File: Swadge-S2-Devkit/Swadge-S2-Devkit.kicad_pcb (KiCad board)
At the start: 2 copper layers, 99.9 x 99.9 mm, 80 parts, among them J1 USB_B_Micro, J2 Conn_01x14_Male, J3 Conn_01x14_Male, J4 Conn_01x14_Male, M1 Motor_DC, Q1 Q_N_FET, Q2 AP2003_PN_FET, Q3 AP2003_PN_FET, Q4 AP2003_PN_FET, SW1 4-1437565-2, SW13 touch-ring-6, SW14 SW_SPDT, SW2 4-1437565-2, SW3 4-1437565-2, SW4 4-1437565-2, SW5 4-1437565-2, SW6 4-1437565-2, SW7 4-1437565-2, SW8 4-1437565-2, SW9 4-1437565-2, U1 ESP32-S2-SOLO, U2 BUS_PCIexpress, U3 AP1117-33, U4 GS321-TR, U5 QMA7981, U6 INGHAi_GSPK2308P-8R0.5W, U7 TFT-1.14, U8 TFT_DISPLAY

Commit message: Update with routing.
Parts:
- added C15: 10μF, Swadge_Parts:C_0603_1608Metric, F.Cu at (131.2, 60.0)
- added R10: 10Ω, Swadge_Parts:R_0603_1608Metric, F.Cu at (111.4, 122.4)
- moved SW14 98.2 mm to (104.5, 113.5), turned to -90 degrees
- moved BT2 55.9 mm to (180.4, 101.5), turned to -90 degrees
- moved BT1 55.8 mm to (124.5, 101.5), turned to 90 degrees
- moved C12 33.9 mm to (139.8, 113.6), turned to 90 degrees
- moved C8 25.7 mm to (110.0, 129.6), turned to 150 degrees
- moved U3 15.5 mm to (118.8, 106.5)
- moved C7 13.7 mm to (118.8, 100.5)
- moved R7 11.3 mm to (103.6, 136.7), turned to -90 degrees
- moved L2 5.58 mm to (148.8, 88.2), turned to -90 degrees
- moved BTN1 3.79 mm to (125.0, 91.2), turned to 180 degrees
- moved C13 3.74 mm to (136.7, 110.3), turned to -90 degrees
- moved C2 3.37 mm to (135.5, 54.3), turned to 90 degrees
- moved R12 1.65 mm to (142.0, 107.6), turned to -90 degrees
- moved R11 1.43 mm to (139.8, 107.5), turned to -90 degrees
- moved C17 1.31 mm to (152.3, 86.8)
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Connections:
- net Net-(BT1-Pad1) renamed BATTMID
- net Net-(BT2-Pad1) renamed BATTPLUS
- C8 pad 2: +3V3 -> Net-(C8-Pad2)
- C9 pad 2: +3V3 -> Net-(C8-Pad2)
- R5 pad 2: +3V3 -> Net-(C8-Pad2)
- R7 pad 1: +3V3 -> Net-(C8-Pad2)
- U2 pad A12: MOTOR -> unconnected-(U2-PadA12)
- U2 pad A13: SPK -> unconnected-(U2-PadA13)
- U2 pad A14: BZR -> unconnected-(U2-PadA14)
- U2 pad B12: MOTOR -> unconnected-(U2-PadB12)
- U2 pad B13: SPK -> unconnected-(U2-PadB13)
- U2 pad B14: BZR -> unconnected-(U2-PadB14)
- U4 pad 5: +3V3 -> Net-(C8-Pad2)
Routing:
- net GND: track 0.00 -> 620.9 mm, vias 0 -> 50
- net +3V3: track 5.11 -> 348.5 mm, vias 0 -> 11
- net TX: track 0.00 -> 179.1 mm, vias 0 -> 3
- net RX: track 0.00 -> 178.5 mm, vias 0 -> 3
- net MIC: track 0.00 -> 150.9 mm, vias 0 -> 2
- net BTN_2: track 0.00 -> 131.4 mm, vias 0 -> 4
- net BTN_7: track 0.00 -> 125.8 mm, vias 0 -> 3
- net SCL: track 0.00 -> 120.7 mm, vias 0 -> 5
- net TFT_CS: track 0.00 -> 113.5 mm, vias 0 -> 6
- net SDA: track 0.00 -> 113.4 mm, vias 0 -> 5
- net BTN_6: track 0.00 -> 112.3 mm, vias 0 -> 1
- net BTN_1: track 0.00 -> 108.6 mm, vias 0 -> 4
- net BTN_8: track 0.00 -> 106.3 mm
- net LED: track 0.00 -> 105.6 mm, vias 0 -> 6
- net TFT_RESET: track 0.00 -> 98.7 mm, vias 0 -> 8
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
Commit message: Update design.
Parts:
- removed R21: 0Ω, Swadge_Parts:R_0603_1608Metric
- removed R22: NP, Swadge_Parts:R_0603_1608Metric
- added J5: MICSEL, Swadge_Parts:PinHeader_1x03_P2.54mm_Vertical, F.Cu at (117.5, 142.9)
- added J6: TRYMIC, Swadge_Parts:PinSocket_1x02_P2.54mm_Vertical, F.Cu at (120.0, 147.5)
- added R23: 10Ω, Swadge_Parts:R_0603_1608Metric, F.Cu at (188.7, 56.2)
- C1, C2, C3, R1: moved to B.Cu
- J2: value Conn_01x14_Male -> DEBUG_BANK_C; footprint Swadge_Parts:PinHeader_1x14_P1.27mm_Vertical -> Swadge_Parts:PinHeader_2x07_P2.54mm_Vertical; moved to F.Cu
- J3: value Conn_01x14_Male -> DEBUG_BANK_B; footprint Swadge_Parts:PinHeader_1x14_P1.27mm_Vertical -> Swadge_Parts:PinHeader_2x07_P2.54mm_Vertical; moved to F.Cu
- J4: value Conn_01x14_Male -> DEBUG_BANK_A; footprint Swadge_Parts:PinHeader_1x14_P1.27mm_Vertical -> Swadge_Parts:PinHeader_2x07_P2.54mm_Vertical; moved to F.Cu
- R2, R3: value NP -> NP/3.3kΩ
- moved C2 14.2 mm to (149.6, 53.3), turned to 180 degrees
- moved C1 12.7 mm to (149.6, 56.4), turned to 0 degrees
- moved R1 12.1 mm to (149.6, 54.9)
- moved C3 8.27 mm to (147.3, 54.1)
- moved R2 4.26 mm to (135.8, 65.7), turned to 180 degrees
- moved R3 2.97 mm to (135.8, 64.0), turned to 0 degrees
- moved J3 2.50 mm to (144.5, 76.5), turned to 90 degrees
- moved J4 2.29 mm to (139.2, 54.0), turned to 0 degrees
- moved R15 1.93 mm to (149.0, 79.5)
- moved R16 1.93 mm to (150.6, 79.5)
- moved R17 1.93 mm to (152.1, 79.5)
- moved R18 1.93 mm to (153.6, 79.5)
- moved R19 1.93 mm to (155.1, 79.5)
- moved R20 1.93 mm to (156.7, 79.5)
- moved J2 0.71 mm to (165.1, 54.0), turned to 0 degrees
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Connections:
- J2 pad 10: BTN_3 -> TFT_RESET
- J2 pad 11: TFTATN -> TFT_SDA
- J2 pad 12: TFT_CS -> TFT_SCL
- J2 pad 13: TFT_RESET -> TFTATP
- J3 pad 12: TFT_SCL -> TFTATN
- J3 pad 13: TFT_SDA -> TFT_CS
- J3 pad 14: TFTATP -> BTN_3
- J3 pad 2: TFT_LEDA_TRIG -> GND
- LS1 pad 1: BZR -> Net-(LS1-Pad1)
- U1 pad 24: TFT_SCL -> TFTATN
- U1 pad 25: TFT_SDA -> TFT_CS
- U1 pad 26: TFTATP -> BTN_3
- U1 pad 28: TFT_RESET -> TFTATP
- U1 pad 29: TFT_CS -> TFT_SCL
- U1 pad 30: TFTATN -> TFT_SDA
- U1 pad 31: BTN_3 -> TFT_RESET
- U2 pad A2: BTN_11 -> BTN_8
- U2 pad A3: TFT_RESET -> BTN_4
- U2 pad A4: TFT_CS -> BTN_3
- U2 pad A5: MIC -> unconnected-(U2-PadA5)
- U2 pad A6: SCL -> unconnected-(U2-PadA6)
- U2 pad A7: SDA -> unconnected-(U2-PadA7)
- U2 pad B2: BTN_11 -> BTN_8
- U2 pad B3: TFT_RESET -> BTN_4
- U2 pad B4: TFT_CS -> BTN_3
- U2 pad B5: MIC -> unconnected-(U2-PadB5)
- U2 pad B6: SCL -> unconnected-(U2-PadB6)
- U2 pad B7: SDA -> unconnected-(U2-PadB7)
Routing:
- net GND: track 620.9 -> 861.3 mm, vias 50 -> 61
- net TFT_CS: track 113.5 -> 31.5 mm, vias 6 -> 2
- net SCL: track 120.7 -> 51.0 mm, vias 5 -> 3
- net SDA: track 113.4 -> 53.4 mm, vias 5 -> 3
- net MIC: track 150.9 -> 91.5 mm, vias 2 -> 0
- net TFT_RESET: track 98.7 -> 45.7 mm, vias 8 -> 3
- net BTN_8: track 106.3 -> 155.1 mm, vias 0 -> 4
- net BTN_4: track 73.8 -> 109.6 mm, vias 2 -> 5
- net +3V3: track 348.5 -> 382.9 mm, vias 11 -> 15
- net BTN_3: track 97.9 -> 118.6 mm, vias 4 -> 7
- net TFTATN: track 52.9 -> 34.2 mm
- net Net-(R16-Pad1): track 82.1 -> 69.5 mm
- net TFT_SCL: track 32.8 -> 44.4 mm, vias 2 -> 3
- net TFT_SDA: track 35.0 -> 46.6 mm, vias 2 -> 3
- net LED: track 105.6 -> 115.4 mm, vias 6 -> 7
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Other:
- board text added: "+ -"

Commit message: Bump
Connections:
- net Net-(D8-Pad4) renamed 5VIN
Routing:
- net GND: track 861.3 -> 1864.0 mm, vias 61 -> 153
- net TX: track 180.7 -> 174.9 mm
- net RX: track 178.9 -> 173.3 mm
- net BTN_7: track 125.7 -> 130.0 mm
- net 5VIN: track 20.4 -> 17.2 mm
- net +3V3: track 382.9 -> 380.6 mm
- net BTN_2: track 127.0 -> 125.0 mm
- net BTN_8: track 155.1 -> 153.2 mm
- net BTN_5: track 51.2 -> 49.5 mm
- net BATTMID: track 61.5 -> 60.4 mm
- net LED: track 115.4 -> 114.3 mm
- net Net-(D8-Pad3): track 39.5 -> 38.5 mm
- net BTN_4: track 109.6 -> 108.7 mm
- net Net-(D8-Pad2): track 36.3 -> 35.6 mm
- net SP-: track 54.2 -> 53.5 mm
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
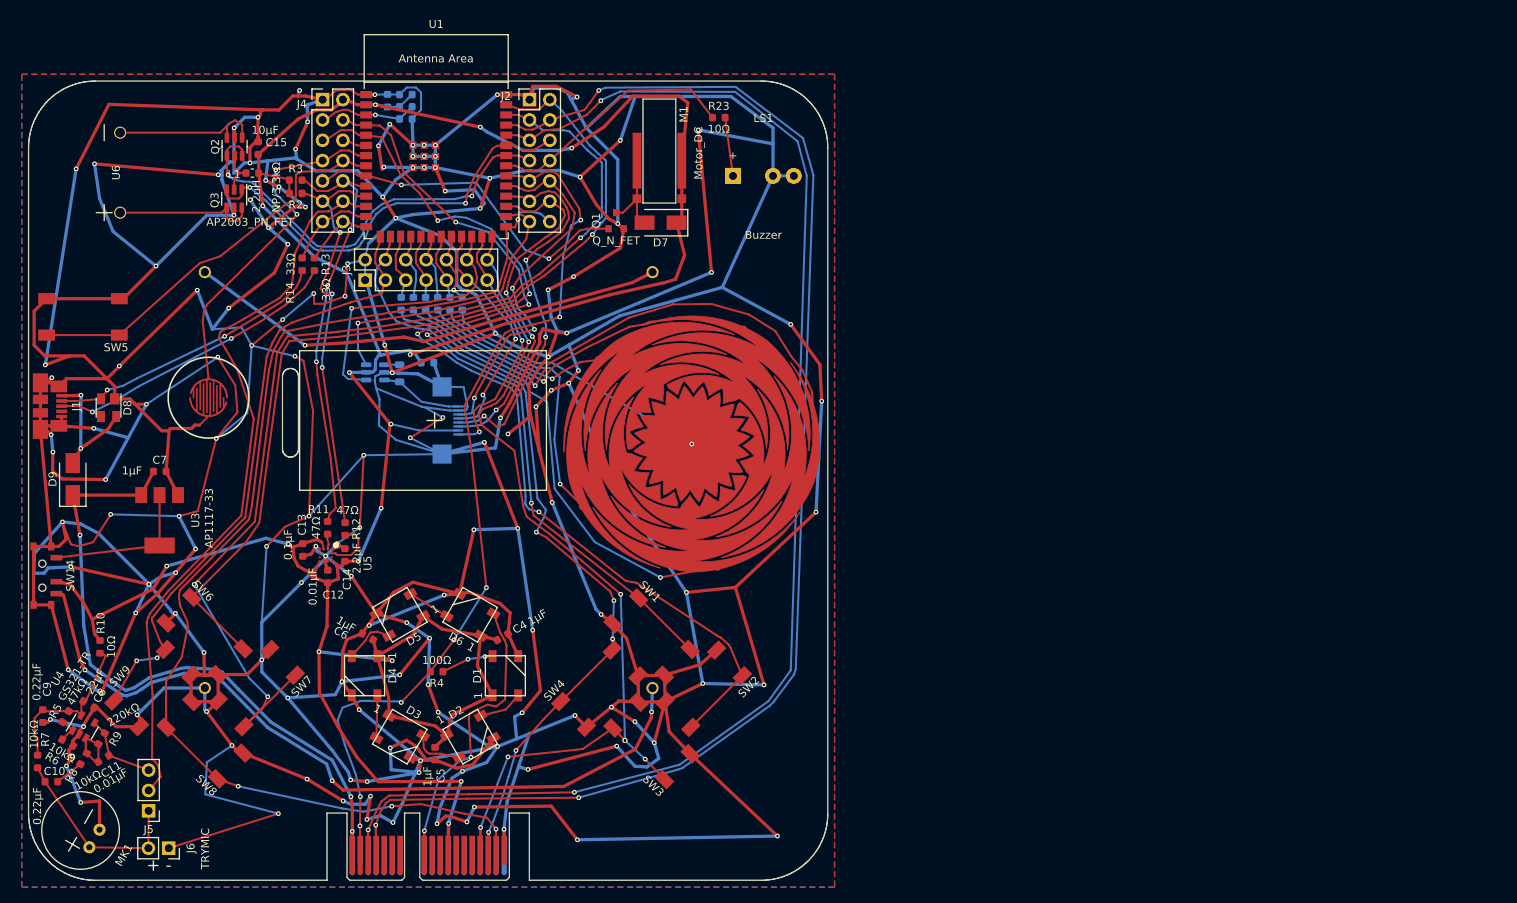
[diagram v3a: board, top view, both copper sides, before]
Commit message: Bump design with new LCDs, etc.
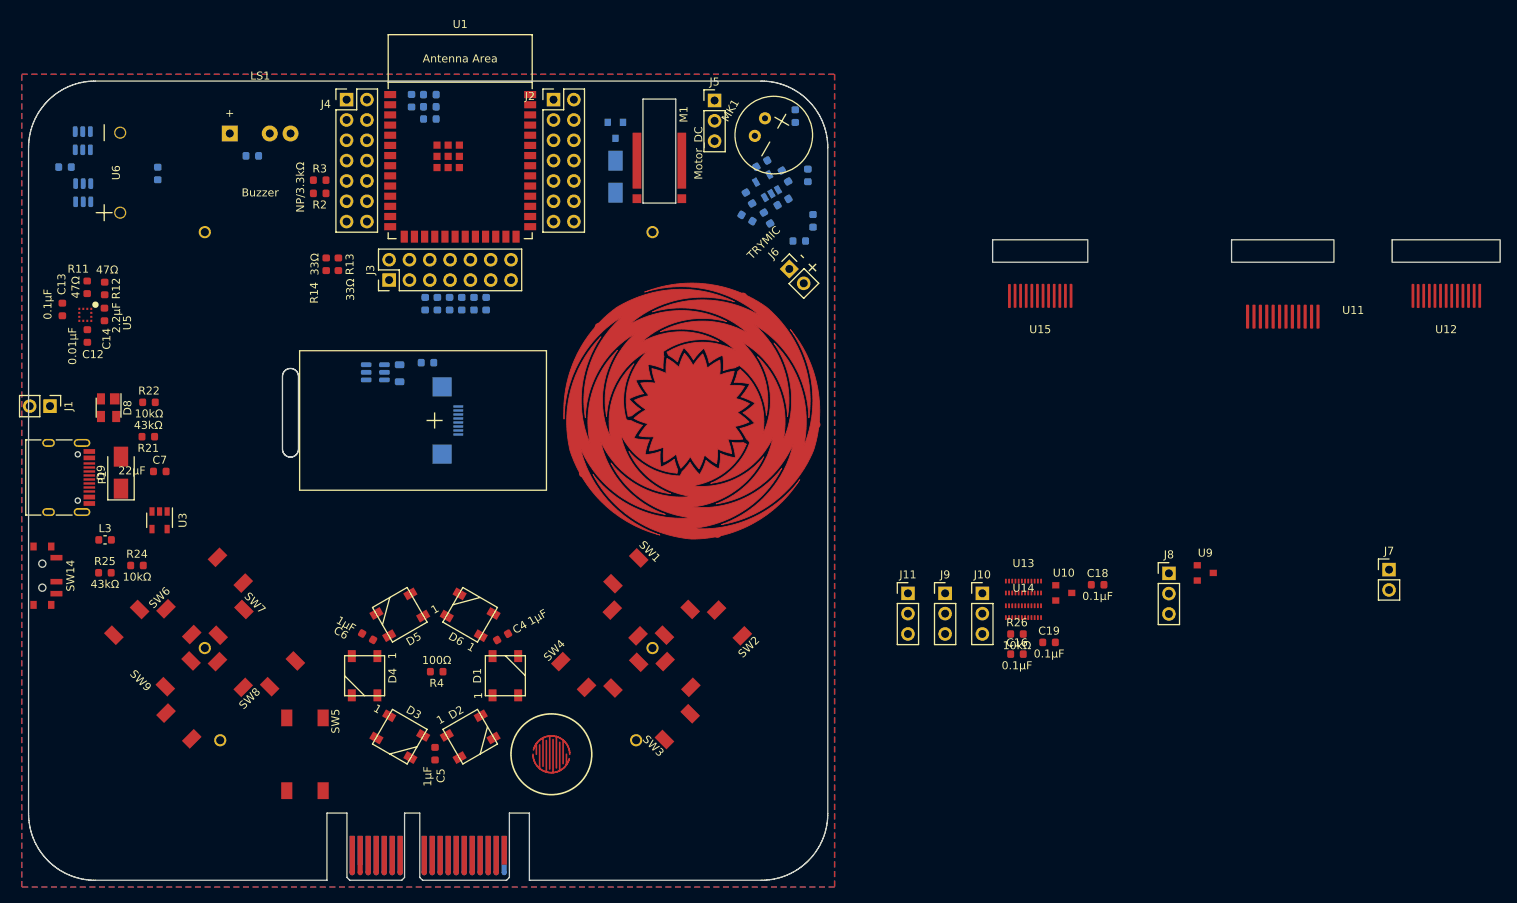
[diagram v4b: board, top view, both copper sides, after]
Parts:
- added BT3: Battery, Swadge_Parts:2460, B.Cu at (152.4, 134.0)
- added C16: 0.1μF, Swadge_Parts:C_0603_1608Metric, F.Cu at (226.0, 123.3)
- added C18: 0.1μF, Swadge_Parts:C_0603_1608Metric, F.Cu at (236.1, 114.6)
- added C19: 0.1μF, Swadge_Parts:C_0603_1608Metric, F.Cu at (230.0, 121.8)
- added J10: IM0, Swadge_Parts:PinHeader_1x03_P2.54mm_Vertical, F.Cu at (221.7, 115.7)
- added J11: IM1, Swadge_Parts:PinHeader_1x03_P2.54mm_Vertical, F.Cu at (212.4, 115.7)
- added J7: LEDK_J, Swadge_Parts:PinHeader_1x02_P2.54mm_Vertical, F.Cu at (272.5, 112.7)
- added J8: IM0, Swadge_Parts:PinHeader_1x03_P2.54mm_Vertical, F.Cu at (245.0, 113.2)
- added J9: IM1, Swadge_Parts:PinHeader_1x03_P2.54mm_Vertical, F.Cu at (217.0, 115.7)
- added L3: 2.2uH, Swadge_Parts:L_0603_1608Metric, F.Cu at (112.0, 109.0)
- added P1: USB_C_Plug_USB2.0, Swadge_Parts:USB_C_Receptacle_HRO_TYPE-C-31-M-12, F.Cu at (106.0, 101.2)
- added R21: 43kΩ, Swadge_Parts:R_0603_1608Metric, F.Cu at (117.4, 96.1)
- added R22: 10kΩ, Swadge_Parts:R_0603_1608Metric, F.Cu at (117.5, 91.8)
- added R24: 10kΩ, Swadge_Parts:R_0603_1608Metric, F.Cu at (116.0, 112.2)
- added R25: 43kΩ, Swadge_Parts:R_0603_1608Metric, F.Cu at (112.0, 113.1)
- added R26: 10kΩ, Swadge_Parts:R_0603_1608Metric, F.Cu at (226.0, 120.8)
- added U10: GENERIC_LDO_GOI, Swadge_Parts:SOT-23, F.Cu at (231.8, 115.6)
- added U11: LCD_240x240_1.3_12, Swadge_Parts:LCD_240x240_1.3_12, F.Cu at (256.8, 81.1)
- added U12: LCD_135x240_1.14_13, Swadge_Parts:LCD_135x240_1.14_13, F.Cu at (279.6, 78.5)
- added U13: LCD_240x240_1.3_24, Swadge_Parts:BM20B(0.8)-24DP-0.4V, F.Cu at (226.8, 114.9)
- added U14: LCD_240x240_1.54_24, Swadge_Parts:BM20B(0.8)-24DP-0.4V, F.Cu at (226.8, 118.0)
- added U15: LCD_240x240_1.54_12, Swadge_Parts:LCD_240x240_1.54_12, F.Cu at (228.9, 78.5)
- added U9: GENERIC_LDO_1.8, Swadge_Parts:SOT-23, F.Cu at (249.5, 113.1)
- C10, C11, C15, C8, C9, D7, L1, Q1, Q2, Q3, R10, R23, R5, R6, R7, R8, R9, U4: moved to B.Cu
- C7: value 1μF -> 22μF
- J1: value USB_B_Micro -> CurrentMonitor; footprint Swadge_Parts:USB_Micro-B_Molex_47346-0001 -> Swadge_Parts:PinHeader_1x02_P2.54mm_Vertical
- U3: value AP1117-33 -> MT3410; footprint Swadge_Parts:SOT-223-3_TabPin2 -> Swadge_Parts:SOT-23-5
- moved MK1 122.7 mm to (195.6, 58.4), turned to -120 degrees
- moved R7 118.2 mm to (200.5, 69.1)
- moved C9 117.1 mm to (199.9, 63.4)
- moved C10 115.4 mm to (198.8, 71.6), turned to 0 degrees
- moved J5 113.5 mm to (188.2, 54.1), turned to 0 degrees
- moved R5 112.5 mm to (197.0, 63.5), turned to 120 degrees
- moved R6 112.1 mm to (196.8, 66.8), turned to 30 degrees
- moved R10 109.3 mm to (198.3, 56.0)
- moved R8 108.9 mm to (194.8, 68.8), turned to -60 degrees
- moved U4 108.9 mm to (194.8, 64.8), turned to 120 degrees
- moved C8 107.9 mm to (194.1, 62.0), turned to 30 degrees
- moved J6 106.1 mm to (197.5, 75.1), turned to 45 degrees
- moved R9 105.4 mm to (192.5, 66.3), turned to -60 degrees
- moved C11 105.1 mm to (192.3, 68.8), turned to -30 degrees
- moved LS1 63.1 mm to (127.6, 58.2)
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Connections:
- BT2 pad 1: BATTPLUS -> BATTMID2
- C7 pad 1: +5V -> Net-(SW14-Pad2)
- J1 pad 1: 5VIN -> Net-(SW14-Pad1)
- J1 pad 2: Net-(D8-Pad2) -> +5V
- J3 pad 10: TOUCH_6 -> TFT_RESET
- J3 pad 5: TOUCH_1 -> LCD_FMARK
- J3 pad 6: TOUCH_2 -> TFT_LEDA
- J3 pad 7: TOUCH_3 -> unconnected-(J3-Pad7)
- J3 pad 8: TOUCH_4 -> TFT_IM1
- J3 pad 9: TOUCH_5 -> TFT_IM0
- R13 pad 2: Net-(D8-Pad3) -> Net-(D8-Pad2)
- R14 pad 2: Net-(D8-Pad2) -> Net-(D8-Pad3)
- SW14 pad 2: +3V3 -> Net-(SW14-Pad2)
- U3 pad 1: GND -> Net-(SW14-Pad2)
- U3 pad 2: Net-(SW14-Pad1) -> GND
- U3 pad 3: +5V -> Net-(L3-Pad2)
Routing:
- net GND: track 1864.0 -> 0.00 mm, vias 153 -> 0
- net +3V3: track 380.6 -> 0.00 mm, vias 15 -> 0
- net TX: track 174.9 -> 0.00 mm, vias 3 -> 0
- net RX: track 173.3 -> 0.00 mm, vias 3 -> 0
- net BTN_8: track 153.2 -> 0.00 mm, vias 4 -> 0
- net BTN_7: track 130.0 -> 0.00 mm, vias 3 -> 0
- net BTN_2: track 125.0 -> 0.00 mm, vias 4 -> 0
- net BTN_3: track 118.5 -> 0.00 mm, vias 7 -> 0
- net LED: track 114.3 -> 0.00 mm, vias 7 -> 0
- net BTN_6: track 112.6 -> 0.00 mm, vias 1 -> 0
- net BTN_4: track 108.7 -> 0.00 mm, vias 5 -> 0
- net BTN_1: track 103.5 -> 0.00 mm, vias 4 -> 0
- net BATTPLUS: track 96.2 -> 0.00 mm, vias 3 -> 0
- net MIC: track 91.2 -> 0.00 mm
- net +5V: track 84.4 -> 0.00 mm, vias 3 -> 0
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
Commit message: Bump - with bigger outline
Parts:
- J10: value IM0 -> LCD18
- J11: value IM1 -> LCD28
- U11, U12, U15: moved to B.Cu
- moved U7 75.9 mm to (225.4, 123.6), turned to 0 degrees
- moved C17 72.4 mm to (218.9, 58.4)
- moved L2 72.4 mm to (215.4, 59.7)
- moved Q4 72.4 mm to (212.4, 59.6)
- moved U9 62.8 mm to (190.4, 134.1), turned to 90 degrees
- moved J7 61.6 mm to (211.4, 120.6)
- moved U12 58.2 mm to (225.3, 99.4), turned to 180 degrees
- moved U10 51.5 mm to (190.4, 146.1), turned to 90 degrees
- moved U13 50.3 mm to (228.4, 64.6), turned to 90 degrees
- moved C18 48.4 mm to (190.2, 130.1), turned to 180 degrees
- moved J8 48.4 mm to (204.4, 139.5)
- moved C19 44.5 mm to (190.4, 142.1), turned to 180 degrees
- moved C16 42.5 mm to (186.4, 138.8), turned to -90 degrees
- moved U11 39.1 mm to (218.0, 85.8), turned to 180 degrees
- moved U14 35.4 mm to (228.4, 82.6), turned to 90 degrees
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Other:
- board size 99.9 x 99.9 mm -> 134 x 100 mm

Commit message: Bump with routing
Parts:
- R26: moved to B.Cu
- moved R26 49.6 mm to (162.5, 80.2), turned to -90 degrees
- moved J1 24.4 mm to (107.6, 116.5)
- moved R4 13.6 mm to (153.6, 111.9)
- moved C15 13.2 mm to (106.3, 58.4)
- moved D9 13.0 mm to (105.7, 110.6)
- moved SW14 9.66 mm to (104.8, 123.1)
- moved R24 8.28 mm to (122.0, 106.5), turned to -90 degrees
- moved R25 8.16 mm to (119.2, 109.3), turned to 180 degrees
- moved C17 6.96 mm to (212.1, 57.0)
- moved C12 5.74 mm to (107.9, 78.1), turned to 180 degrees
- moved D8 5.51 mm to (116.0, 96.7)
- moved R21 4.96 mm to (121.2, 99.3), turned to -90 degrees
- moved R22 4.95 mm to (121.1, 95.2), turned to 90 degrees
- moved L3 4.84 mm to (116.1, 106.4), turned to 90 degrees
- moved C7 2.59 mm to (120.2, 102.7), turned to 180 degrees
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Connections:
- J3 pad 10: TFT_RESET -> unconnected-(J3-Pad10)
- J3 pad 5: LCD_FMARK -> unconnected-(J3-Pad5)
- J3 pad 6: TFT_LEDA -> unconnected-(J3-Pad6)
- J3 pad 8: TFT_IM1 -> unconnected-(J3-Pad8)
- J3 pad 9: TFT_IM0 -> unconnected-(J3-Pad9)
- U1 pad 6: SPARE1 -> VMON
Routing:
- net GND: track 0.00 -> 789.5 mm, vias 0 -> 35
- net +3V3: track 0.00 -> 482.9 mm, vias 0 -> 19
- net BTN_8: track 0.00 -> 143.7 mm, vias 0 -> 4
- net TFT_CS: track 0.00 -> 131.4 mm, vias 0 -> 4
- net TFT_RESET: track 0.00 -> 125.2 mm, vias 0 -> 4
- net BTN_2: track 0.00 -> 124.1 mm, vias 0 -> 2
- net TFT_SCL: track 0.00 -> 121.0 mm, vias 0 -> 2
- net TFT_SDA: track 0.00 -> 120.2 mm, vias 0 -> 3
- net BTN_3: track 0.00 -> 114.9 mm, vias 0 -> 4
- net TX: track 0.00 -> 113.1 mm, vias 0 -> 2
- net LED: track 0.00 -> 112.4 mm, vias 0 -> 4
- net TFT_LEDA: track 0.00 -> 111.4 mm, vias 0 -> 7
- net RX: track 0.00 -> 110.6 mm, vias 0 -> 2
- net BTN_5: track 0.00 -> 107.9 mm, vias 0 -> 2
- net BLISTER1: track 0.00 -> 103.2 mm, vias 0 -> 4
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
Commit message: Update as initial rev -
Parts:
- removed J9: IM1, Swadge_Parts:PinHeader_1x03_P2.54mm_Vertical
- removed U13: LCD_240x240_1.3_24, Swadge_Parts:BM20B(0.8)-24DP-0.4V
- removed U14: LCD_240x240_1.54_24, Swadge_Parts:BM20B(0.8)-24DP-0.4V
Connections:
- U15 pad 7: TFT_IM0 -> TFT_RS
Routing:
- net TFT_IM1: track 96.7 -> 0.00 mm
- net TFT_RS: track 91.2 -> 165.7 mm, vias 2 -> 9
- net TFT_IM0: track 58.4 -> 0.00 mm
- net GND: track 789.5 -> 814.8 mm, vias 35 -> 120
- net +3V3: vias 19 -> 20
